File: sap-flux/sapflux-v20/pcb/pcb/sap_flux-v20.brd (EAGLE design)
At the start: 76.2 x 54.6 mm, 93 parts, among them J1 CON_01X02-0.2"_POL, J2 CON_01X02TINY, J3 CON_01X02TINY, J4 CON_01X02TINY, J5 CON_01X02TINY, Q1 Nfet, Q2 nfet, Q3 pfet, U1 ADP2503, U3 ADP1614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

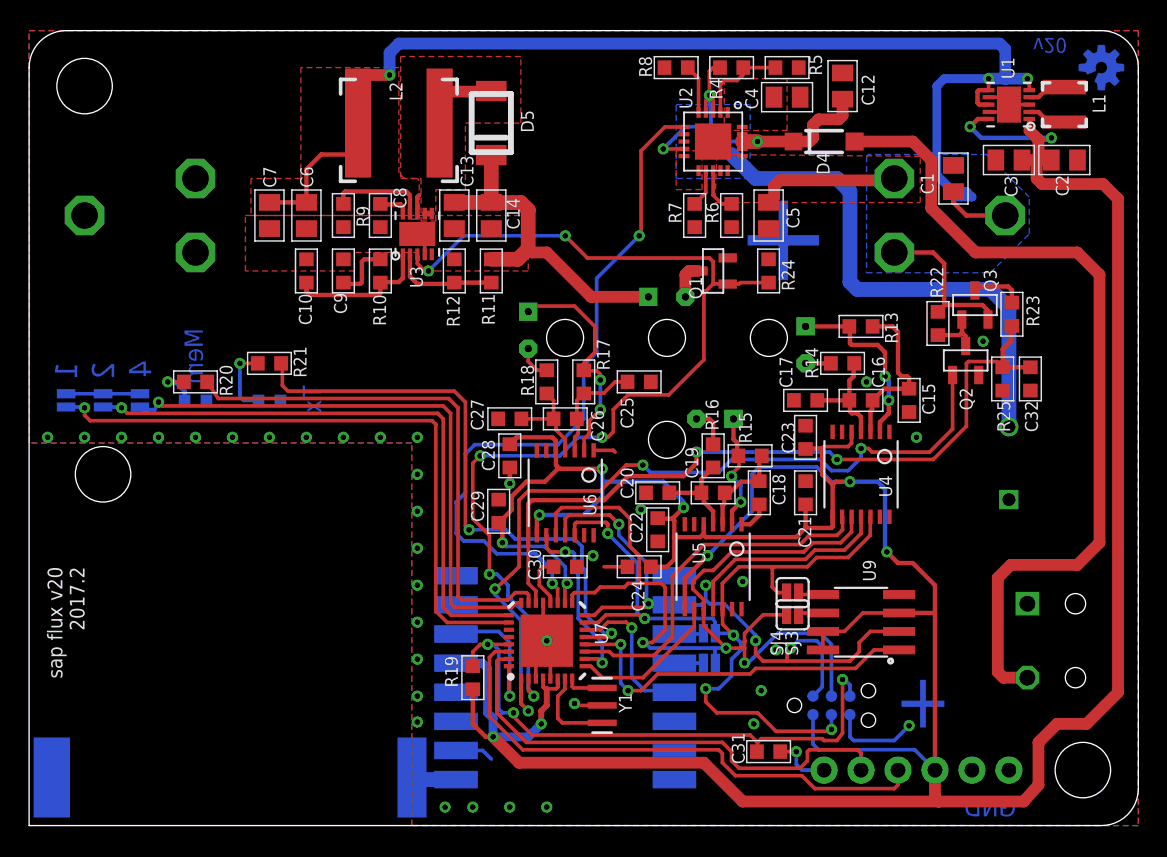
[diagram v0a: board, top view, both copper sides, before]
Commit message: updated bottom Silk Screen
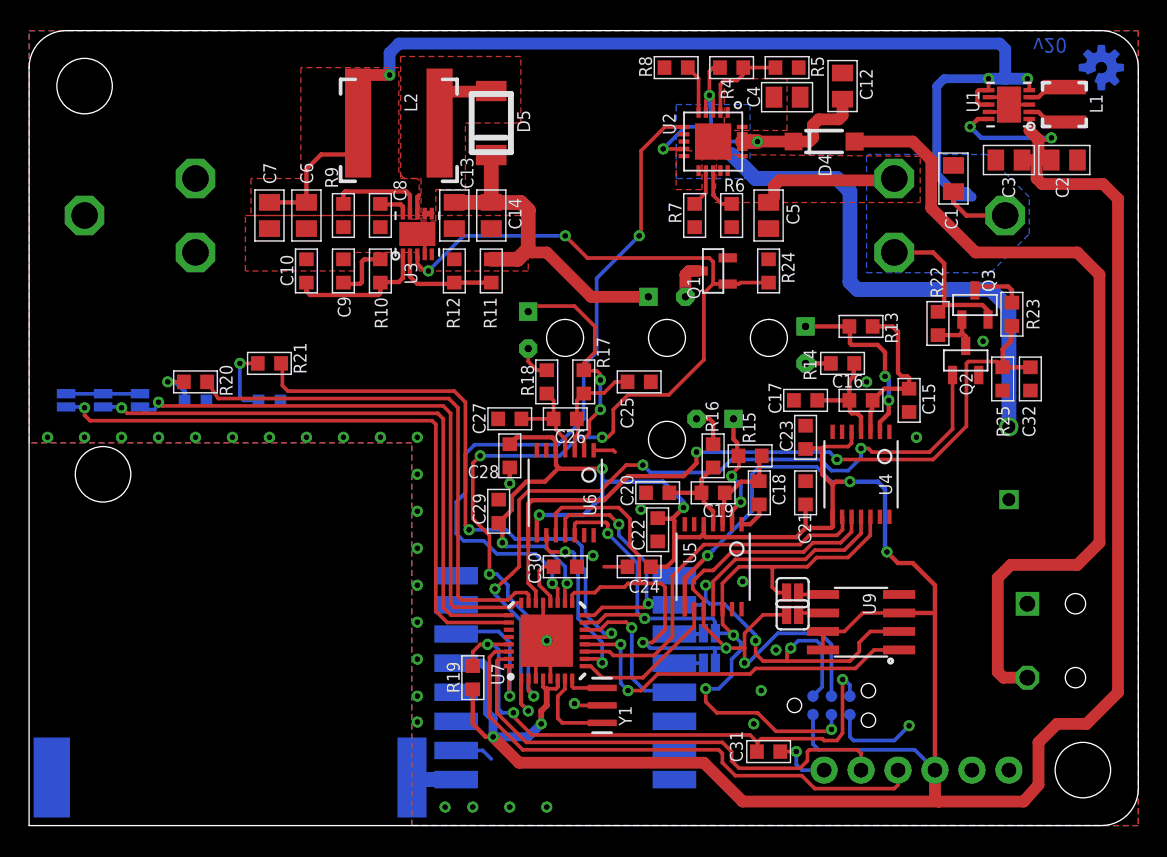
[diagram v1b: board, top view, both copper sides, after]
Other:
- board text added: "HEAT"
- board text added: "NETWORK"
- board text added: "NODE ID"
- board text added: "TC1"
- board text added: "TC2"
- board text added: "TC3"
